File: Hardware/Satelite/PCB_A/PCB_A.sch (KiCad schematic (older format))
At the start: 33 parts, among them J1 Batería LiPo (Soldada), J2 CONUFL001-SMD, J3 Servo Globo, J4 Conector_PCB_A-B, J5 Servo Paracaídas, M1 Spacer, M2 Spacer, M3 Spacer, Q1 SSM3J338R,LF, Q2 BC817, U4 AP9211SA-AF-HAC-7

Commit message: Completado nuevo PCB_A
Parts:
- removed TP3: TestPoint_P1, TestPoint:TestPoint_Pad_D1.0mm, symbol Connector:TestPoint_Probe
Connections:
- wire segments 93 -> 92
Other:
- moved on the sheet: TP1, TP2, TP4, TP5
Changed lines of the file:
@@
 L power:+BATT #PWR014
 U 1 1 5C2D3F1A
-P 5050 1100
-F 0 "#PWR014" H 5050 950 50  0001 C CNN
-F 1 "+BATT" H 5064 1275 50  0000 C CNN
-F 2 "" H 5050 1100 50  0001 C CNN
-F 3 "" H 5050 1100 50  0001 C CNN
-	1    5050 1100
+P 4950 1100
+F 0 "#PWR014" H 4950 950 50  0001 C CNN
+F 1 "+BATT" H 4964 1275 50  0000 C CNN
+F 2 "" H 4950 1100 50  0001 C CNN
+F 3 "" H 4950 1100 50  0001 C CNN
+	1    4950 1100
 	1    0    0    -1
 $EndComp
@@
 L Connector:TestPoint_Probe TP2
 U 1 1 5C2DEC1A
-P 5050 1400
-F 0 "TP2" H 5800 1550 50  0000 R CNN
-F 1 "TestPoint_GPSTX" H 5800 1450 50  0000 R CNN
-F 2 "TestPoint:TestPoint_Pad_D1.0mm" H 5250 1400 50  0001 C CNN
-F 3 "~" H 5250 1400 50  0001 C CNN
-	1    5050 1400
+P 4950 1400
+F 0 "TP2" H 5700 1550 50  0000 R CNN
+F 1 "TestPoint_GPSTX" H 5700 1450 50  0000 R CNN
+F 2 "TestPoint:TestPoint_Pad_D1.0mm" H 5150 1400 50  0001 C CNN
+F 3 "~" H 5150 1400 50  0001 C CNN
+	1    4950 1400
 	-1   0    0    -1
 $EndComp
 Wire Wire Line
-	5050 1400 5350 1400
-Text Label 5150 1400 0    50   ~ 0
+	4950 1400 5350 1400
+Text Label 5350 1400 2    50   ~ 0
 GPS_TX
 $Comp
-L Connector:TestPoint_Probe TP3
-U 1 1 5C2E59E7
-P 5050 1600
-F 0 "TP3" H 5800 1750 50  0000 R CNN
-F 1 "TestPoint_P1" H 5800 1650 50  0000 R CNN
-F 2 "TestPoint:TestPoint_Pad_D1.0mm" H 5250 1600 50  0001 C CNN
-F 3 "~" H 5250 1600 50  0001 C CNN
-	1    5050 1600
+L Connector:TestPoint_Probe TP4
+U 1 1 5C2E7A24
+P 4950 1600
+F 0 "TP4" H 5700 1750 50  0000 R CNN
+F 1 "TestPoint_P1" H 5700 1650 50  0000 R CNN
+F 2 "TestPoint:TestPoint_Pad_D1.0mm" H 5150 1600 50  0001 C CNN
+F 3 "~" H 5150 1600 50  0001 C CNN
+	1    4950 1600
 	-1   0    0    -1
 $EndComp
 Wire Wire Line
-	5050 1600 5350 1600
-Text Label 5150 1600 0    50   ~ 0
-P1
-$Comp
-L Connector:TestPoint_Probe TP4
-U 1 1 5C2E7A24
-P 5050 1800
-F 0 "TP4" H 5800 1950 50  0000 R CNN
-F 1 "TestPoint_P1" H 5800 1850 50  0000 R CNN
-F 2 "TestPoint:TestPoint_Pad_D1.0mm" H 5250 1800 50  0001 C CNN
-F 3 "~" H 5250 1800 50  0001 C CNN
-	1    5050 1800
-	-1   0    0    -1
-$EndComp
-Wire Wire Line
-	5050 1800 5350 1800
+	4950 1600 5350 1600
 $Comp
 L Connector:TestPoint_Probe TP5
 U 1 1 5C2E94B0
-P 5050 2000
-F 0 "TP5" H 5800 2150 50  0000 R CNN
-F 1 "TestPoint_P1" H 5800 2050 50  0000 R CNN
-F 2 "TestPoint:TestPoint_Pad_D1.0mm" H 5250 2000 50  0001 C CNN
-F 3 "~" H 5250 2000 50  0001 C CNN
-	1    5050 2000
+P 4950 1800
+F 0 "TP5" H 5700 1950 50  0000 R CNN
+F 1 "TestPoint_P1" H 5700 1850 50  0000 R CNN
+F 2 "TestPoint:TestPoint_Pad_D1.0mm" H 5150 1800 50  0001 C CNN
+F 3 "~" H 5150 1800 50  0001 C CNN
+	1    4950 1800
 	-1   0    0    -1
 $EndComp
-Text Label 5100 1800 0    50   ~ 0
+Text Label 5350 1600 2    50   ~ 0
 S_GLOBO
-Text Label 5600 2000 2    50   ~ 0
+Text Label 5500 1800 2    50   ~ 0
 S_PARACAIDAS
 Wire Wire Line
-	5050 2000 5600 2000
+	4950 1800 5500 1800
 Wire Wire Line
 	5950 2050 5950 2000
 Wire Wire Line
-	5050 1100 5050 1200
+	4950 1100 4950 1200
 $Comp
 L Connector:TestPoint_Probe TP1
 U 1 1 5C2FCED2
-P 5050 1200
-F 0 "TP1" H 5800 1350 50  0000 R CNN
-F 1 "TestPoint_BATT" H 5800 1250 50  0000 R CNN
-F 2 "TestPoint:TestPoint_Pad_D1.0mm" H 5250 1200 50  0001 C CNN
-F 3 "~" H 5250 1200 50  0001 C CNN
-	1    5050 1200
+P 4950 1200
+F 0 "TP1" H 5700 1350 50  0000 R CNN
+F 1 "TestPoint_BATT" H 5700 1250 50  0000 R CNN
+F 2 "TestPoint:TestPoint_Pad_D1.0mm" H 5150 1200 50  0001 C CNN
+F 3 "~" H 5150 1200 50  0001 C CNN
+	1    4950 1200
 	-1   0    0    -1
 $EndComp

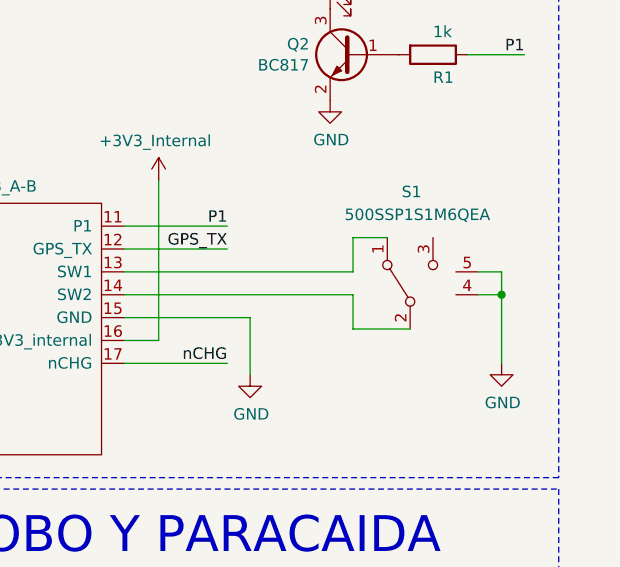
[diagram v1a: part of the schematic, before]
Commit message: Mejoras al layout RF de PCB_A
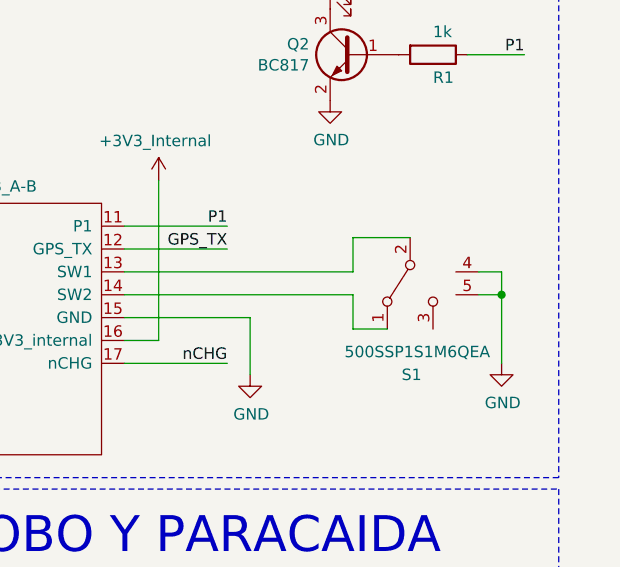
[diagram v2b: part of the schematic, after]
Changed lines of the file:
@@
 F 8 "500SSP1S1M6QEA" H 11150 2200 50  0001 L CNN "Arrow Part Number"
 	1    10500 2900
-	0    -1   -1   0
+	0    -1   1    0
 $EndComp
 $Comp
@@
 	10200 2850 10200 2700
 Wire Wire Line
-	10200 2700 10350 2700
+	10200 2700 10450 2700
 Wire Wire Line
 	9200 2950 10200 2950
@@
 	10200 2950 10200 3100
 Wire Wire Line
-	10200 3100 10450 3100
+	10200 3100 10350 3100
 $Comp
 L power:GND #PWR046

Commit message: Eliminidas tiras de pines en PCB_A para conexión de servos, se sueldan los cables directamente al PCB
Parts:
- J3, J5: Manufacturer Part Number 61300311121 -> (none)
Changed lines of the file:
@@
 F 2 "Connector_PinHeader_2.54mm:PinHeader_1x03_P2.54mm_Vertical" H 9600 5050 50  0001 C CNN
 F 3 "~" H 9600 5050 50  0001 C CNN
-F 4 "61300311121" H 9600 5050 50  0001 C CNN "Manufacturer Part Number"
 	1    9600 5050
 	0    -1   -1   0
@@
 F 2 "Connector_PinHeader_2.54mm:PinHeader_1x03_P2.54mm_Vertical" H 8150 5050 50  0001 C CNN
 F 3 "~" H 8150 5050 50  0001 C CNN
-F 4 "61300311121" H 8150 5050 50  0001 C CNN "Manufacturer Part Number"
 	1    8150 5050
 	0    -1   -1   0
